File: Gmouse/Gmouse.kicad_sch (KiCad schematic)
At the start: 1 part, among them U1 Teensy4.0

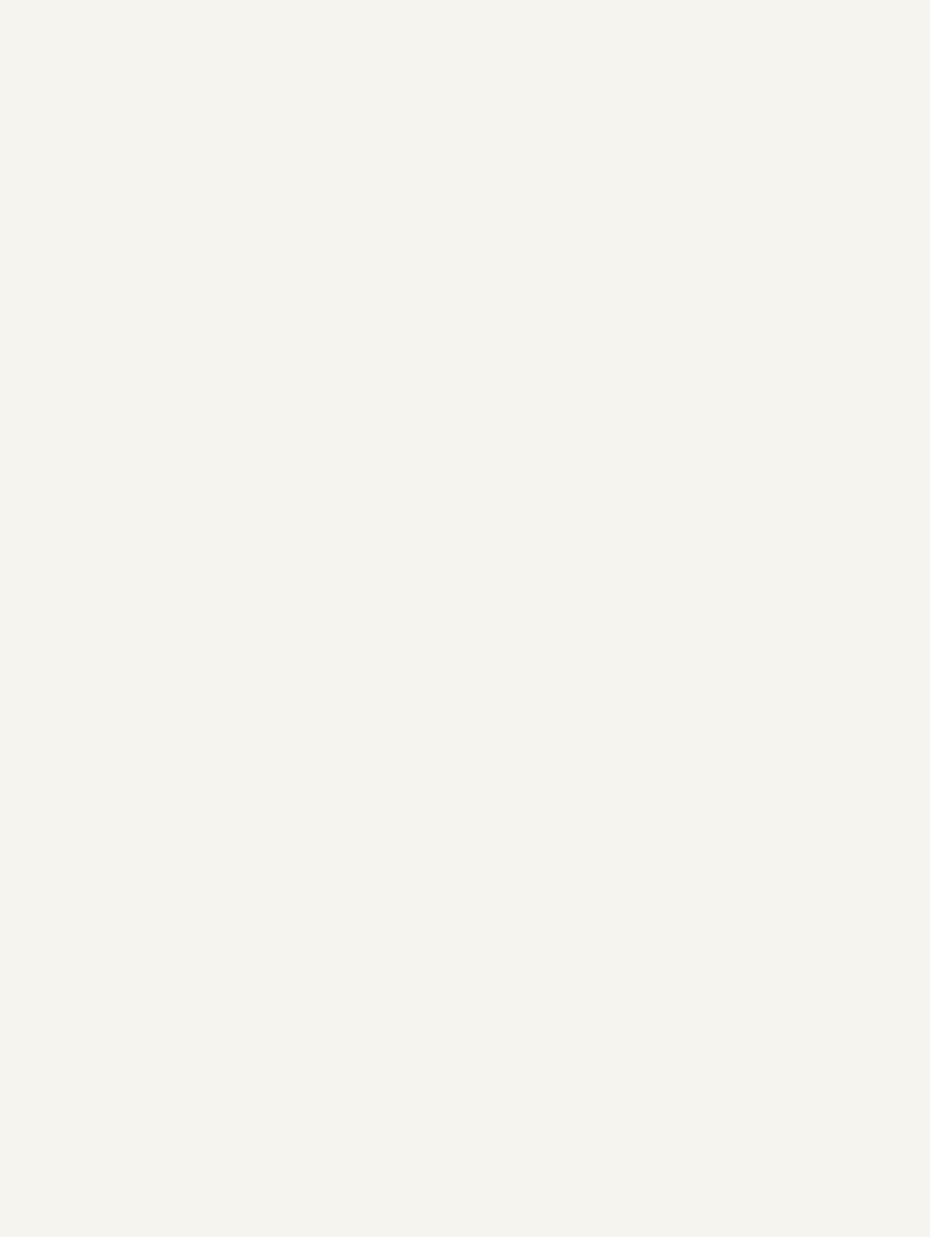
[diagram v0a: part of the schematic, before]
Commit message: Added some motors and motor drivers to schematic
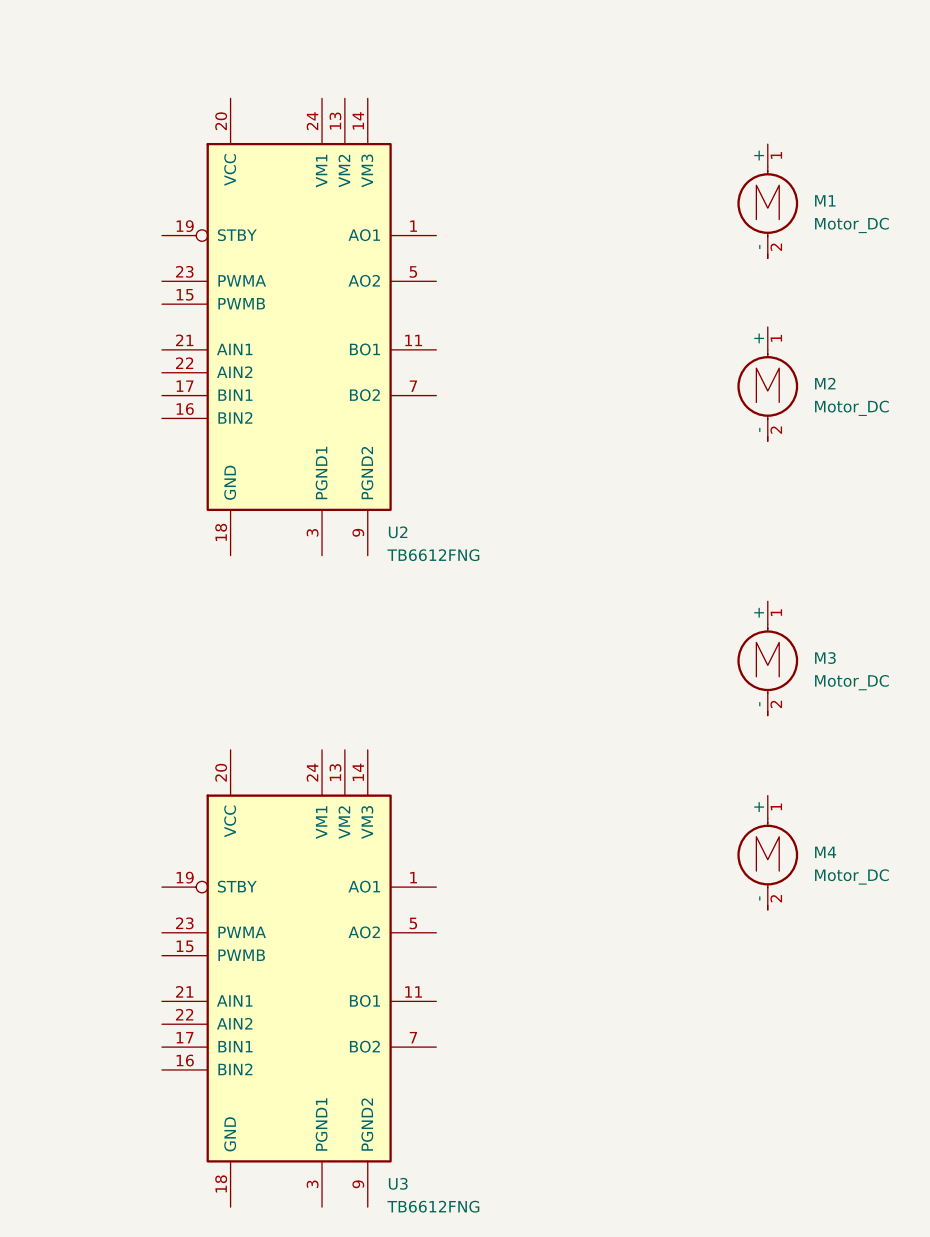
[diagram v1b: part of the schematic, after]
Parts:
- added M1, M2, M3, M4: Motor_DC, symbol Motor:Motor_DC
- added U2, U3: TB6612FNG, Package_SO:SSOP-24_5.3x8.2mm_P0.65mm, symbol Driver_Motor:TB6612FNG
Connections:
- new net: U3.1 (AO1), U3.2 (AO1)
- new net: U3.10 (PGND2), U3.9 (PGND2)
- new net: U3.11 (BO1), U3.12 (BO1)
- new net: U3.3 (PGND1), U3.4 (PGND1)
- new net: U3.5 (AO2), U3.6 (AO2)
- new net: U3.7 (BO2), U3.8 (BO2)
- new net: U2.1 (AO1), U2.2 (AO1)
- new net: U2.10 (PGND2), U2.9 (PGND2)
- new net: U2.11 (BO1), U2.12 (BO1)
- new net: U2.3 (PGND1), U2.4 (PGND1)
- new net: U2.5 (AO2), U2.6 (AO2)
- new net: U2.7 (BO2), U2.8 (BO2)

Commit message: Adds basic motor circuitry and connectors, includes LED Display
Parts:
- removed M1, M2, M3, M4: Motor_DC, symbol Motor:Motor_DC
- removed U3: TB6612FNG, Package_SO:SSOP-24_5.3x8.2mm_P0.65mm, symbol Driver_Motor:TB6612FNG
- added BT1: 6V, symbol Device:Battery_Cell
- added C1, C3: 10 uF, symbol Device:C_Polarized
- added C2, C4: 0.1 uF, symbol Device:C
- added J1: Motor 1, symbol Connector:Conn_01x06_Pin
- added J2: Motor 2, symbol Connector:Conn_01x06_Pin
- added U3: L78L05_SOT89, Package_TO_SOT_SMD:SOT-89-3, symbol Regulator_Linear:L78L05_SOT89
- added U4: HCMS-2903, DIP12_HCMS-290X-A_BRA, symbol HCMS_2903:HCMS-2903
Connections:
- net Motor1_M1: now reaches U2.1 (AO1), U2.2 (AO1)
- net Motor1_M1: now also J1.6 (Pin_6)
- net GND: now reaches U2.10 (PGND2), U2.9 (PGND2)
- net GND: now also U2.18 (GND), U2.3 (PGND1), U2.4 (PGND1), BT1.2 (-), C1.2, C2.2, C3.2, C4.2, J1.1 (Pin_1), J2.1 (Pin_1), U3.2 (GND)
- net Motor2_M1: now reaches U2.11 (BO1), U2.12 (BO1)
- net Motor2_M1: now also J2.6 (Pin_6)
- net +BATT: now reaches U2.13 (VM2)
- net +BATT: now also U2.14 (VM3), U2.24 (VM1), BT1.1 (+), C1.1, C2.1, U3.3 (IN)
- net +5V: now reaches U2.20 (VCC)
- net +5V: now also C3.1, C4.1, J1.4 (Pin_4), J2.4 (Pin_4), U3.1 (OUT)
- net Motor1_M2: now reaches U2.5 (AO2), U2.6 (AO2)
- net Motor1_M2: now also J1.5 (Pin_5)
- net Motor2_M2: now reaches U2.7 (BO2), U2.8 (BO2)
- net Motor2_M2: now also J2.5 (Pin_5)
- new net Motor1_OutA: J1.3 (Pin_3)
- new net Motor1_OutB: J1.2 (Pin_2)
- new net Motor2_OutA: J2.3 (Pin_3)
- new net Motor2_OutB: J2.2 (Pin_2)
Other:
- moved on the sheet: U2

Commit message: Added some pins
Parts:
- added C5: 4.7uF, symbol Device:C_Small
- added C6: 0.1uF, symbol Device:C_Small
- added D1: IR, symbol Device:LED
- added Q1: NMOS, symbol Simulation_SPICE:NMOS
- added Q2: SFH300, LED_THT:LED_D5.0mm_Clear, symbol Sensor_Optical:SFH300
- added R1: 47K, symbol Device:R
- added R2: 100, symbol Device:R
- added R3: 51, symbol Device:R
- added R4: 1.8K, symbol Device:R
- added U7: LD1117S33TR_SOT223, Package_TO_SOT_SMD:SOT-223-3_TabPin2, symbol Regulator_Linear:LD1117S33TR_SOT223
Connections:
- net +5V: now also U4.3 (V_LED)
- net GND: now also U4.9 (GND), C5.2, C6.2, Q1.3 (S), R1.2
- new net: Q2.2 (E), R4.1
- new net: Q1.2 (G), R1.1, R2.2
- new net: D1.2 (A), R3.2
- new net: D1.1 (K), Q1.1 (D)
- new net +3V3: C5.1, C6.1, Q2.1 (C), R3.1
- no-connect marks 0 -> 12
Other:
- note added: "IR Emitter Circuit"
- note added: "IR Reciever Circuit"

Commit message: Work Done Over Break
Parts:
- added BT2: 3.7V, Connector_JST:JST_PH_B2B-PH-K_1x02_P2.00mm_Vertical, symbol Device:Battery_Cell
- added C10, C8: 10 uF, symbol Device:C_Polarized
- added C11, C13, C15, C17, C19: 4.7uF, Capacitor_SMD:C_1206_3216Metric_Pad1.33x1.80mm_HandSolder, symbol Device:C_Small
- added C12, C14, C16, C18, C20: 0.1uF, Capacitor_SMD:C_1206_3216Metric_Pad1.33x1.80mm_HandSolder, symbol Device:C_Small
- added C7, C9: 0.1 uF, Capacitor_SMD:C_1206_3216Metric_Pad1.33x1.80mm_HandSolder, symbol Device:C
- added D2, D3, D4, D5, D6: IR, LED_THT:LED_D5.0mm_Horizontal_O1.27mm_Z9.0mm, symbol Device:LED
- added D7: D, symbol Device:D
- added J3: Motor_LF, Connector_JST:JST_SH_BM05B-SRSS-TB_1x05-1MP_P1.00mm_Vertical, symbol Connector:Conn_01x06_Pin
- added J4: Motor_LR, Connector_JST:JST_SH_BM05B-SRSS-TB_1x05-1MP_P1.00mm_Vertical, symbol Connector:Conn_01x06_Pin
- added J5: Conn_01x08_Pin, Connector_PinSocket_2.54mm:PinSocket_1x08_P2.54mm_Vertical, symbol Connector:Conn_01x08_Pin
- added LS1: SMT-0440-T-R, SMT_0440:XDCR_SMT-0440-T-R, symbol SMT_Speaker:SMT-0440-T-R
- added Q10, Q12, Q4, Q6, Q8: SFH300, LED_THT:LED_D5.0mm_Horizontal_O1.27mm_Z3.0mm_IRGrey, symbol Sensor_Optical:SFH300
- added Q11, Q3, Q5, Q7, Q9: NMOS, symbol Simulation_SPICE:NMOS
- added Q14: BC847, Package_TO_SOT_SMD:SOT-23, symbol Transistor_BJT:BC847
- added R10, R14, R18, R22, R6: 47K, Resistor_SMD:R_1206_3216Metric_Pad1.30x1.75mm_HandSolder, symbol Device:R
- added R11, R15, R19, R23, R7: 51, Resistor_SMD:R_1206_3216Metric_Pad1.30x1.75mm_HandSolder, symbol Device:R
- added R12, R16, R20, R24, R8: 1.8K, Resistor_SMD:R_1206_3216Metric_Pad1.30x1.75mm_HandSolder, symbol Device:R
- added R13, R17, R21, R5, R9: 100, Resistor_SMD:R_1206_3216Metric_Pad1.30x1.75mm_HandSolder, symbol Device:R
- added R25: 180, Resistor_SMD:R_1206_3216Metric_Pad1.30x1.75mm_HandSolder, symbol Device:R
- added R26, R27: R, symbol Device:R
- added S1, S2: TL3365AF180QG, TL3365AF180QG:SW_TL3365AF180QG, symbol Buttons:TL3365AF180QG
- added SW1: SW_SPDT, symbol Switch:SW_SPDT
- added U5: TB6612FNG, Package_SO:SSOP-24_5.3x8.2mm_P0.65mm, symbol Driver_Motor:TB6612FNG
- BT1: value 6V -> 3.7V; footprint (none) -> Connector_JST:JST_PH_B2B-PH-K_1x02_P2.00mm_Vertical
- C2, C4, C5, C6: footprint (none) -> Capacitor_SMD:C_1206_3216Metric_Pad1.33x1.80mm_HandSolder
- D1: footprint (none) -> LED_THT:LED_D5.0mm_Horizontal_O1.27mm_Z9.0mm
- J1: value Motor 1 -> Motor_RF; footprint (none) -> Connector_JST:JST_SH_BM05B-SRSS-TB_1x05-1MP_P1.00mm_Vertical
- J2: value Motor 2 -> Motor_RR; footprint (none) -> Connector_JST:JST_SH_BM05B-SRSS-TB_1x05-1MP_P1.00mm_Vertical
- Q2: footprint LED_THT:LED_D5.0mm_Clear -> LED_THT:LED_D5.0mm_Horizontal_O1.27mm_Z3.0mm_IRGrey
- R1, R2, R3, R4: footprint (none) -> Resistor_SMD:R_1206_3216Metric_Pad1.30x1.75mm_HandSolder
- U4: footprint DIP12_HCMS-290X-A_BRA -> HCMS_2903:DIP12_HCMS-290X-A_BRA
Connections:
- net +3V3: now also U7.2 (VO), C11.1, C12.1, C13.1, C14.1, C15.1, C16.1, C17.1, C18.1, C19.1, C20.1, D7.1 (K), LS1.P, Q10.1 (C), Q12.1 (C), Q4.1 (C), Q6.1 (C), Q8.1 (C), R11.1, R15.1, R19.1, R23.1, R7.1, S1.1, S1.2, S2.1, S2.2
- net +5V: now also U1.33 (VIN), U4.10 (SEL), U4.11 (V_LOGIC), C7.1, C8.1, J3.4 (Pin_4), J4.4 (Pin_4), U5.20 (VCC)
- net +BATT: now also U7.3 (VI), C10.1, C9.1, SW1.3 (C), U5.13 (VM2), U5.14 (VM3), U5.24 (VM1); no longer BT1.1 (+)
- net GND: now also R4.2, U1.1 (GND), U1.17 (GND), U1.32 (GND), U4.8 (BLANK), U7.1 (GND), BT2.2 (-), C10.2, C11.2, C12.2, C13.2, C14.2, C15.2, C16.2, C17.2, C18.2, C19.2, C20.2, C7.2, C8.2, C9.2, J3.1 (Pin_1), J4.1 (Pin_1), Q11.3 (S), Q14.2 (E), Q3.3 (S), Q5.3 (S), Q7.3 (S), Q9.3 (S), R10.2, R12.2, R14.2, R16.2, R18.2, R20.2, R22.2, R24.2, R26.1, R27.2, R6.2, R8.2, U5.10 (PGND2), U5.18 (GND), U5.3 (PGND1), U5.4 (PGND1), U5.9 (PGND2); no longer BT1.2 (-)
- net IR_Reciever_Left_90: now reaches Q2.2 (E), R4.1
- net IR_Emmiter_Left_Half: now reaches U1.4 (2_OUT2)
- net IR_Emmiter_Left_Half: now also R2.1, R5.1, R9.1
- net IR_Emmiter_Right_Half: now reaches U1.5 (3_LRCLK2)
- net IR_Emmiter_Right_Half: now also R13.1, R17.1, R21.1
- net HCMS_Reset: now reaches U4.12 (*RESET)
- net HCMS_DataIn: now reaches U4.4 (DATA_IN)
- net HCMS_RS: now reaches U4.5 (RS)
- net HCMS_CLK: now reaches U4.6 (CLK)
- net HCMS_CE: now reaches U4.7 (*CE)
- net Motor2_PWM: now reaches U2.15 (PWMB)
- net Right_IN2: now reaches U2.16 (BIN2)
- net Right_IN2: now also U2.22 (AIN2)
- net Right_IN1: now reaches U2.17 (BIN1)
- net Right_IN1: now also U2.21 (AIN1)
- net Motor_STBY: now reaches U2.19 (STBY)
- net Motor_STBY: now also U5.19 (STBY)
- net Motor1_PWM: now reaches U2.23 (PWMA)
- new net: Q11.2 (G), R21.2, R22.1
- new net: Q7.2 (G), R13.2, R14.1
- new net: Q3.2 (G), R5.2, R6.1
- new net: D3.2 (A), R11.2
- new net: BT1.1 (+), SW1.2 (B)
- new net: D5.1 (K), Q9.1 (D)
- new net: D5.2 (A), R19.2
- new net: Q5.2 (G), R10.1, R9.2
- new net: D4.1 (K), Q7.1 (D)
- new net: D4.2 (A), R15.2
- new net: R26.2, S1.4
- new net: D6.1 (K), Q11.1 (D)
- new net: D2.1 (K), Q3.1 (D)
- new net: D2.2 (A), R7.2
- new net: Q14.1 (B), R25.2
- new net: D7.2 (A), LS1.N, Q14.3 (C)
- new net: D6.2 (A), R23.2
- new net: Q9.2 (G), R17.2, R18.1
- new net: D3.1 (K), Q5.1 (D)
- new net: R27.1, S2.4
- new net: BT1.2 (-), BT2.1 (+)
- new net IR_Reciever_Left_0: Q6.2 (E), R12.1
- new net IR_Reciever_Left_45: Q4.2 (E), R8.1
- new net IR_Reciever_Right_0: Q8.2 (E), R16.1
- new net IR_Reciever_Right_45: Q10.2 (E), R20.1
- new net IR_Reciever_Right_90: Q12.2 (E), R24.1
- new net Interface_Button1: S1.3
- new net Interface_Button2: S2.3
- new net Left_IN1: U5.17 (BIN1), U5.21 (AIN1)
- new net Left_IN2: U5.16 (BIN2), U5.22 (AIN2)
- new net Motor_LF_M1: J3.6 (Pin_6), U5.1 (AO1), U5.2 (AO1)
- new net Motor_LF_M2: J3.5 (Pin_5), U5.5 (AO2), U5.6 (AO2)
- new net Motor_LF_OutA: J3.3 (Pin_3)
- new net Motor_LF_OutB: J3.2 (Pin_2)
- new net Motor_LF_PWM: U5.23 (PWMA)
- new net Motor_LR_M1: J4.6 (Pin_6), U5.11 (BO1), U5.12 (BO1)
- new net Motor_LR_M2: J4.5 (Pin_5), U5.7 (BO2), U5.8 (BO2)
- new net Motor_LR_OutA: J4.3 (Pin_3)
- new net Motor_LR_OutB: J4.2 (Pin_2)
- new net Motor_LR_PWM: U5.15 (PWMB)
- new net Speaker Signal: R25.1
- no-connect marks 12 -> 25
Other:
- note added: "Buzzer Circuit"
- note added: "CSB"
- note added: "HCMS LED Display"
- note added: "IR Left Half Circuitry"
- note added: "IR Right Half Circuitry"
- note added: "Interface Buttons"
- note added: "Left Motors"
- note added: "Power Supply"
- note added: "Right Motors"
- note added: "VIN"
- moved on the sheet: BT1, C1, C2, C3, C4, C5, C6, D1, J1, J2, Q1, Q2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

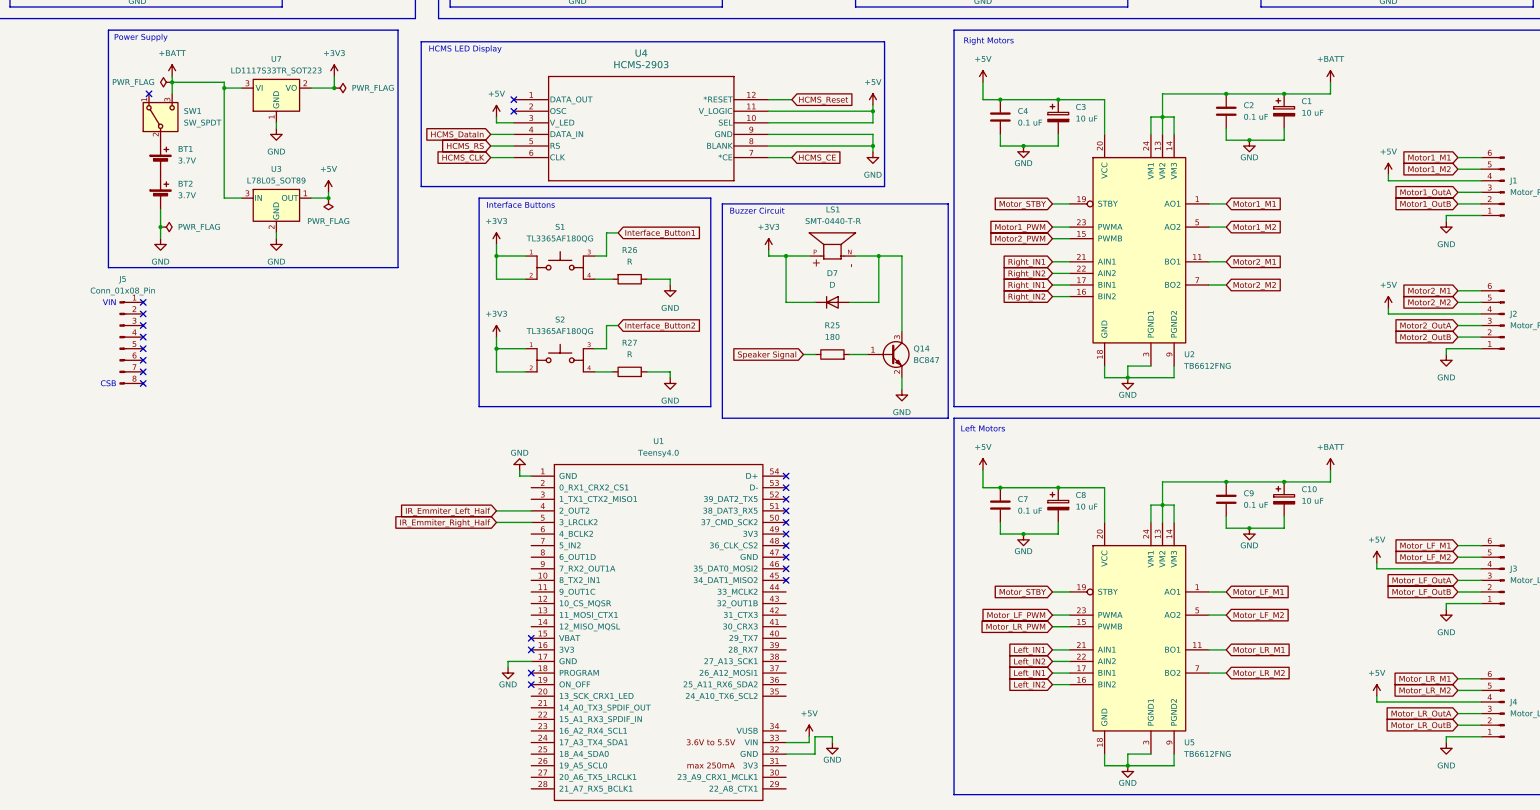
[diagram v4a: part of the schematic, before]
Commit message: starts pcb design and assigns ton of pins
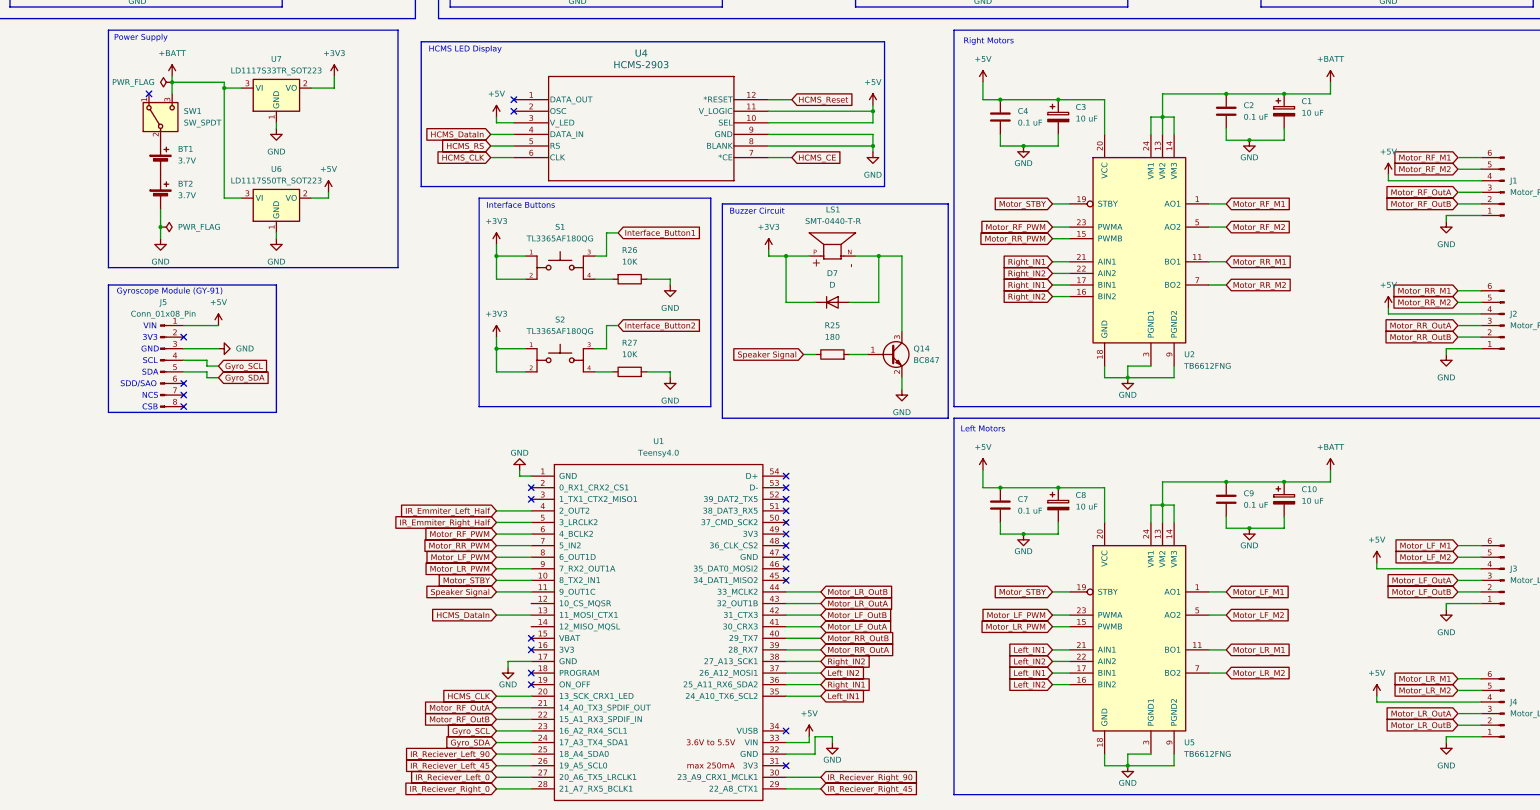
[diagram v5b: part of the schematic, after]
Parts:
- removed U3: L78L05_SOT89, Package_TO_SOT_SMD:SOT-89-3, symbol Regulator_Linear:L78L05_SOT89
- added U6: LD1117S50TR_SOT223, Package_TO_SOT_SMD:SOT-223-3_TabPin2, symbol Regulator_Linear:LD1117S50TR_SOT223
- D1, D2, D3, D4, D5, D6: footprint LED_THT:LED_D5.0mm_Horizontal_O1.27mm_Z9.0mm -> LED_THT:LED_D5.0mm_Horizontal_O3.81mm_Z9.0mm
- J1, J2, J3, J4: footprint Connector_JST:JST_SH_BM05B-SRSS-TB_1x05-1MP_P1.00mm_Vertical -> Connector_JST:JST_SH_BM06B-SRSS-TB_1x06-1MP_P1.00mm_Vertical
- R26, R27: value R -> 10K; footprint (none) -> Resistor_SMD:R_1206_3216Metric_Pad1.30x1.75mm_HandSolder
- S1, S2: footprint TL3365AF180QG:SW_TL3365AF180QG -> Buttons:SW_TL3365AF180QG
- SW1: footprint (none) -> Switch:SW_500SSP1S1M6QEA
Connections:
- net Motor1_OutA is gone; now on net Motor_RF_OutA: J1.3 (Pin_3)
- net Motor1_OutB is gone; now on net Motor_RF_OutB: J1.2 (Pin_2)
- net Motor1_PWM is gone; now on net Motor_RF_PWM: U2.23 (PWMA)
- net Motor2_OutA is gone; now on net Motor_RR_OutA: J2.3 (Pin_3)
- net Motor2_OutB is gone; now on net Motor_RR_OutB: J2.2 (Pin_2)
- net Motor2_PWM is gone; now on net Motor_RR_PWM: U2.15 (PWMB)
- net +5V: now also J5.1 (Pin_1), U6.2 (VO)
- net +BATT: now also U6.3 (VI)
- net GND: now also J5.3 (Pin_3), U6.1 (GND)
- net HCMS_CLK: now also U1.20 (13_SCK_CRX1_LED)
- net HCMS_DataIn: now also U1.13 (11_MOSI_CTX1)
- net IR_Reciever_Left_0: now also U1.27 (20_A6_TX5_LRCLK1)
- net IR_Reciever_Left_45: now also U1.26 (19_A5_SCL0)
- net IR_Reciever_Left_90: now also U1.25 (18_A4_SDA0)
- net IR_Reciever_Right_0: now also U1.28 (21_A7_RX5_BCLK1)
- net IR_Reciever_Right_45: now also U1.29 (22_A8_CTX1)
- net IR_Reciever_Right_90: now also U1.30 (23_A9_CRX1_MCLK1)
- net Left_IN1: now also U1.35 (24_A10_TX6_SCL2)
- net Left_IN2: now also U1.37 (26_A12_MOSI1)
- net Motor_LF_OutA: now also U1.41 (30_CRX3)
- net Motor_LF_OutB: now also U1.42 (31_CTX3)
- net Motor_LF_PWM: now also U1.8 (6_OUT1D)
- net Motor_LR_OutA: now also U1.43 (32_OUT1B)
- net Motor_LR_OutB: now also U1.44 (33_MCLK2)
- net Motor_LR_PWM: now also U1.9 (7_RX2_OUT1A)
- net Motor_STBY: now also U1.10 (8_TX2_IN1)
- net Right_IN1: now also U1.36 (25_A11_RX6_SDA2)
- net Right_IN2: now also U1.38 (27_A13_SCK1)
- net Speaker Signal: now also U1.11 (9_OUT1C)
- net Motor_RF_OutA: now reaches U1.21 (14_A0_TX3_SPDIF_OUT)
- net Motor_RF_OutB: now reaches U1.22 (15_A1_RX3_SPDIF_IN)
- net Gyro_SCL: now reaches U1.23 (16_A2_RX4_SCL1)
- net Gyro_SCL: now also J5.4 (Pin_4)
- net Gyro_SDA: now reaches U1.24 (17_A3_TX4_SDA1)
- net Gyro_SDA: now also J5.5 (Pin_5)
- net Motor_RR_OutA: now reaches U1.39 (28_RX7)
- net Motor_RR_OutB: now reaches U1.40 (29_TX7)
- net Motor_RF_PWM: now reaches U1.6 (4_BCLK2)
- net Motor_RR_PWM: now reaches U1.7 (5_IN2)
- net Motor1_M1 renamed Motor_RF_M1
- net Motor1_M2 renamed Motor_RF_M2
- net Motor2_M1 renamed Motor_RR_M1
- net Motor2_M2 renamed Motor_RR_M2
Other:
- note added: "3V3"
- note added: "GND"
- note added: "Gyroscope Module (GY-91)"
- note added: "NCS"
- note added: "SCL"
- note added: "SDA"
- note added: "SDD/SAO"
- moved on the sheet: J5
